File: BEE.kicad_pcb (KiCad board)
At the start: 2 copper layers, 77.5 x 81.5 mm, 79 parts, among them J1 RPI1_header, J10 Conn_01x02, J11 Conn_01x02, J12 Conn_01x02, J13 Conn_01x06, J14 Conn_01x03, J15 Conn_02x10_Odd_Even, J16 Conn_01x08, J17 Conn_01x05, J18 Conn_01x03, J19 Conn_01x03, J2 Conn_02x05_Odd_Even, J20 Conn_01x10, J21 Conn_01x03, J3 Conn_01x03, J4 Conn_01x06, J5 Conn_02x10_Odd_Even, J6 Conn_01x06, J7 Conn_02x10_Odd_Even, J8 Conn_01x08, J9 Conn_01x02, SW1 SW_Push, SW2 SW_Push, SW3 SW_Push, U1 MCP3008, U2 MCP4911, U3 Dip_10xsp3t, U4 Dip_10xsp3t, U5 74AHC595, U6 Display_7Segments

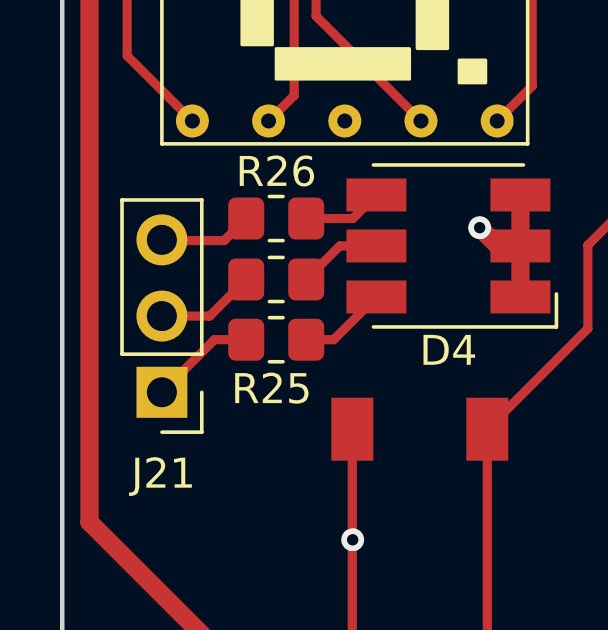
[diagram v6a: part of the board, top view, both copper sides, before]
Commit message: labels for RGB led
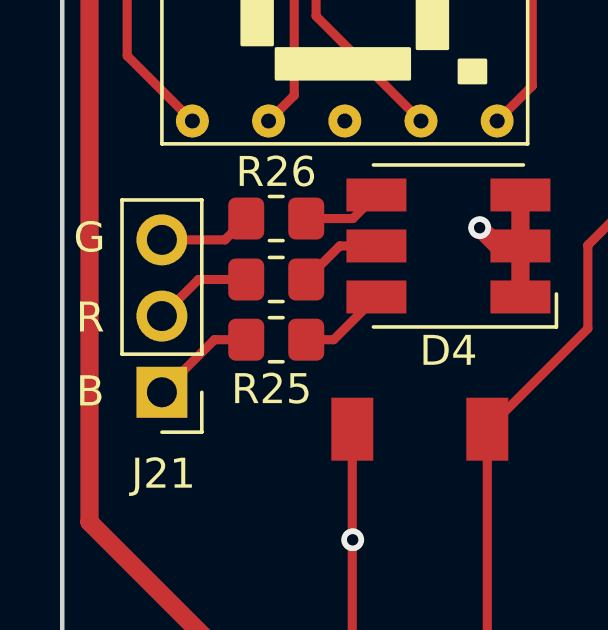
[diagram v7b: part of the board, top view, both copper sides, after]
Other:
- board text added: "B"
- board text added: "G"
- board text added: "R"
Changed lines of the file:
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@@
+    (effects (font (size 1 1) (thickness 0.15)))
+  )
+  (gr_text "R" (at 95.3262 96.266) (layer "F.SilkS")
     (effects (font (size 1 1) (thickness 0.15)))
   )
@@
     (effects (font (size 1 1) (thickness 0.15)))
   )
+  (gr_text "G" (at 95.3008 93.599) (layer "F.SilkS")
+    (effects (font (size 1 1) (thickness 0.15)))
+  )
   (gr_text "B26" (at 97.2566 45.5676) (layer "F.SilkS")
     (effects (font (size 0.75 0.75) (thickness 0.15)))
   )
   (gr_text "High-z" (at 165.8874 96.139) (layer "F.SilkS")
+    (effects (font (size 1 1) (thickness 0.15)))
+  )
+  (gr_text "B" (at 95.3262 98.7298) (layer "F.SilkS")
     (effects (font (size 1 1) (thickness 0.15)))
   )
@@
   (segment (start 102.5238 94.996) (end 103.6414 93.8784) (width 0.3048) (layer "F.Cu") (net 113))
   (segment (start 97.7138 98.7552) (end 99.4664 97.0026) (width 0.3048) (layer "F.Cu") (net 114))
+  (segment (start 97.7138 98.7552) (end 97.7138 98.7298) (width 0.3048) (layer "F.Cu") (net 114))
   (segment (start 99.4664 97.0026) (end 100.5238 97.0026) (width 0.3048) (layer "F.Cu") (net 114))
-  (segment (start 97.7138 96.2152) (end 99.3046 96.2152) (width 0.3048) (layer "F.Cu") (net 115))
-  (segment (start 99.3046 96.2152) (end 100.5238 94.996) (width 0.3048) (layer "F.Cu") (net 115))
+  (segment (start 98.933 94.996) (end 100.5238 94.996) (width 0.3048) (layer "F.Cu") (net 115))
+  (segment (start 97.7138 96.2152) (end 98.933 94.996) (width 0.3048) (layer "F.Cu") (net 115))
+  (segment (start 97.7392 93.6752) (end 97.7646 93.7006) (width 0.3048) (layer "F.Cu") (net 116))
+  (segment (start 99.8126 93.6752) (end 100.5238 92.964) (width 0.3048) (layer "F.Cu") (net 116))
   (segment (start 97.7138 93.6752) (end 97.7392 93.6752) (width 0.3048) (layer "F.Cu") (net 116))
-  (segment (start 97.7392 93.6752) (end 97.7646 93.7006) (width 0.3048) (layer "F.Cu") (net 116))
-  (segment (start 97.7646 93.7006) (end 99.7872 93.7006) (width 0.3048) (layer "F.Cu") (net 116))
-  (segment (start 99.7872 93.7006) (end 100.5238 92.964) (width 0.3048) (layer "F.Cu") (net 116))
+  (segment (start 97.7138 93.6752) (end 99.8126 93.6752) (width 0.3048) (layer "F.Cu") (net 116))
   (segment (start 104.0786 92.964) (end 104.8642 92.1784) (width 0.3048) (layer "F.Cu") (net 121))
   (segment (start 102.5238 92.964) (end 104.0786 92.964) (width 0.3048) (layer "F.Cu") (net 121))

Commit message: BEE 2.0 final touches
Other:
- rule pad_to_mask_clearance: 0.0508 -> 0
